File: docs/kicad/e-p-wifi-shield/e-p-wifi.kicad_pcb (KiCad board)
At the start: 2 copper layers, 76.2 x 86.4 mm, 50 parts, among them J1 Shunt, J2 Vbat1, J3 Masse T1, J4 Température, J5 Vbat2, J6 Conn_02x14_MKR1010, SW1 StSp - Farnell 986-501, SW2 Sleep - Farnell 986-501, SW3 Conrad 711771, SW4 BP APEM - Farnell 108-2512

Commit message: Modifications on pcb
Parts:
- moved LH1 0.64 mm to (76.2, 80.0)
- moved MH1 0.64 mm to (88.3, 58.4)
- moved LH2 0.64 mm to (76.2, 57.1)
- moved MH2 0.64 mm to (88.3, 78.7)
- moved LH3 0.64 mm to (43.2, 68.6)
- moved MH3 0.64 mm to (31.1, 58.4)
- moved MH4 0.64 mm to (31.1, 78.7)
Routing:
- net GND: track 0.00 -> 7.62 mm
- net +3V3: track 125.7 -> 120.5 mm
- net Net-(C6-Pad1): track 97.1 -> 98.5 mm
- net Net-(C2-Pad1): track 55.5 -> 56.8 mm
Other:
- outline, holes or cut-outs redrawn

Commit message: modif pcb
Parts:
- removed V2: Via-DIY, e-p-wifi-v2:Via-DIY
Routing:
- net GND: track 7.62 -> 19.1 mm
- net Net-(J6-PadD1): track 73.7 -> 78.8 mm
- net +3V3: track 120.5 -> 124.3 mm
- net Net-(J6-Pad+5V): track 16.4 -> 18.9 mm
- net Net-(C3-Pad1): track 40.8 -> 43.4 mm
- net Net-(C4-Pad1): track 41.6 -> 43.7 mm
- net Net-(C5-Pad1): track 43.4 -> 41.8 mm
- net Net-(J6-PadD2): track 75.4 -> 76.9 mm
- net Net-(C2-Pad1): track 56.8 -> 58.1 mm
- net Net-(D3-Pad2): track 76.9 -> 76.4 mm
- net Net-(C6-Pad1): track 98.5 -> 99.0 mm

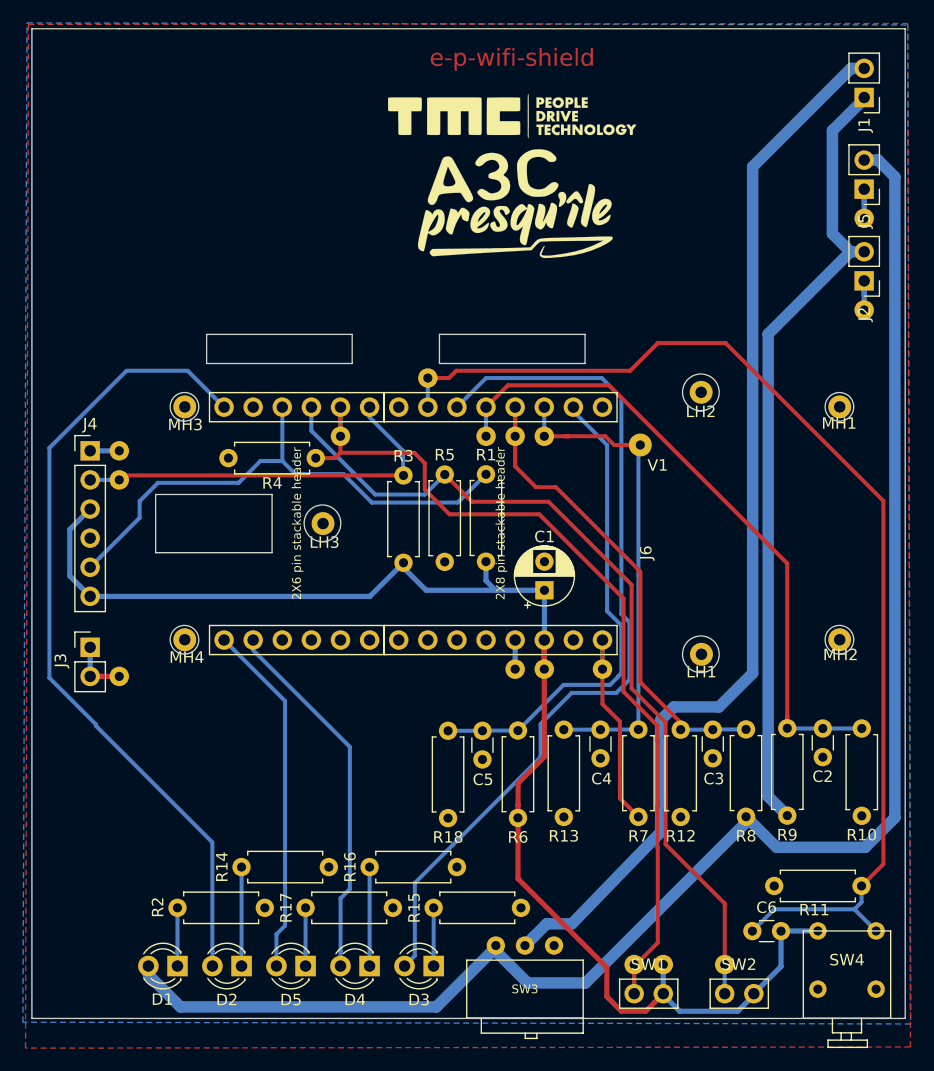
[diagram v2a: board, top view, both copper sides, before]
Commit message: rename 'sans_via' files
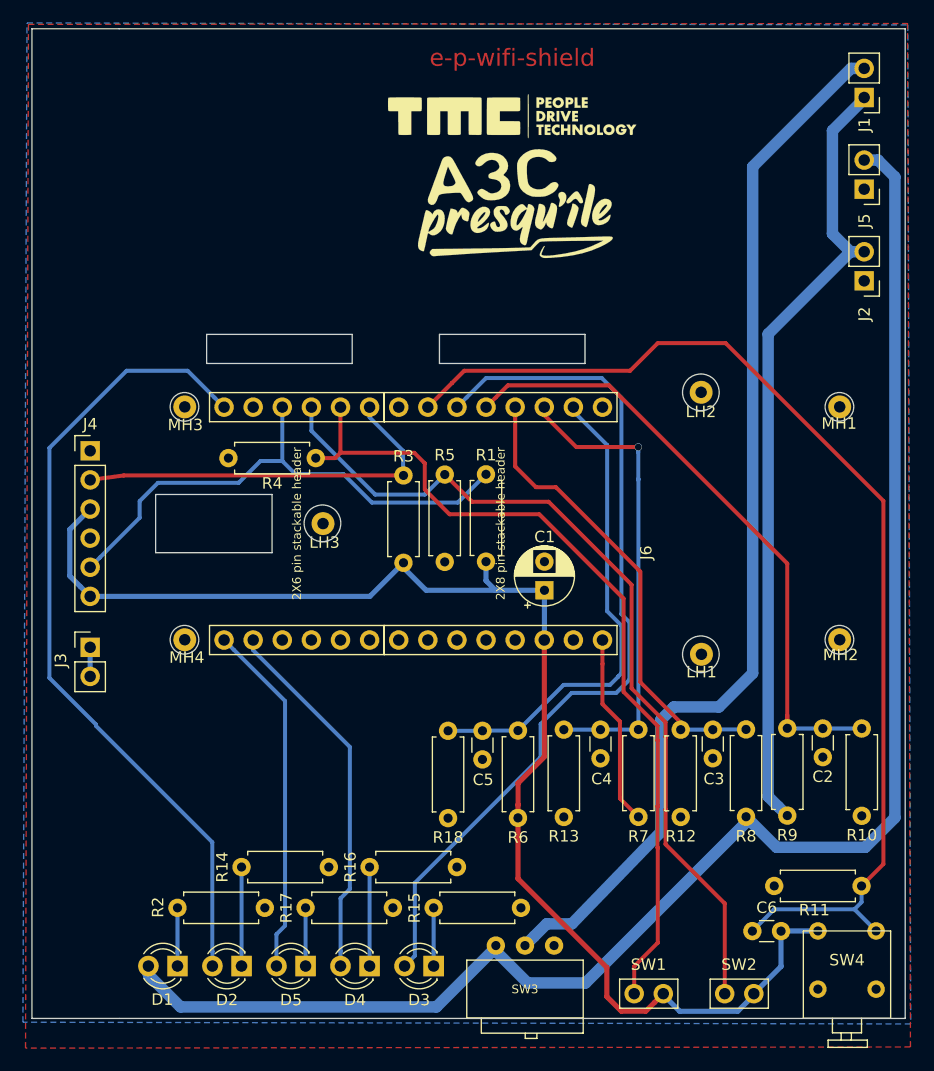
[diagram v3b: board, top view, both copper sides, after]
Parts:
- removed V1: Via, e-p-wifi-v2:Via-DIY
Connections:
- SW4 pad 3: (no net) -> GND
- SW4 pad 4: (no net) -> GND
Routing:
- net GND: track 19.1 -> 2.54 mm
- net Net-(J6-PadD1): track 78.8 -> 73.7 mm
- net +3V3: track 124.3 -> 119.2 mm
- net Net-(J6-Pad+5V): track 18.9 -> 16.4 mm
- net Net-(C3-Pad1): track 43.4 -> 40.8 mm
- net Net-(C2-Pad1): track 58.1 -> 55.5 mm
- net Net-(C4-Pad1): track 43.7 -> 42.0 mm, vias 0 -> 1
- net Net-(C6-Pad1): track 99.0 -> 97.5 mm
